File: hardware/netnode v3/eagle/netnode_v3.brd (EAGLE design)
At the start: 59.9 x 49.9 mm, 29 parts, among them IC1 TSR-1, IC2 PIC18F4K80, IC3 FOD060L, X1 DC10R, X2 XPORT

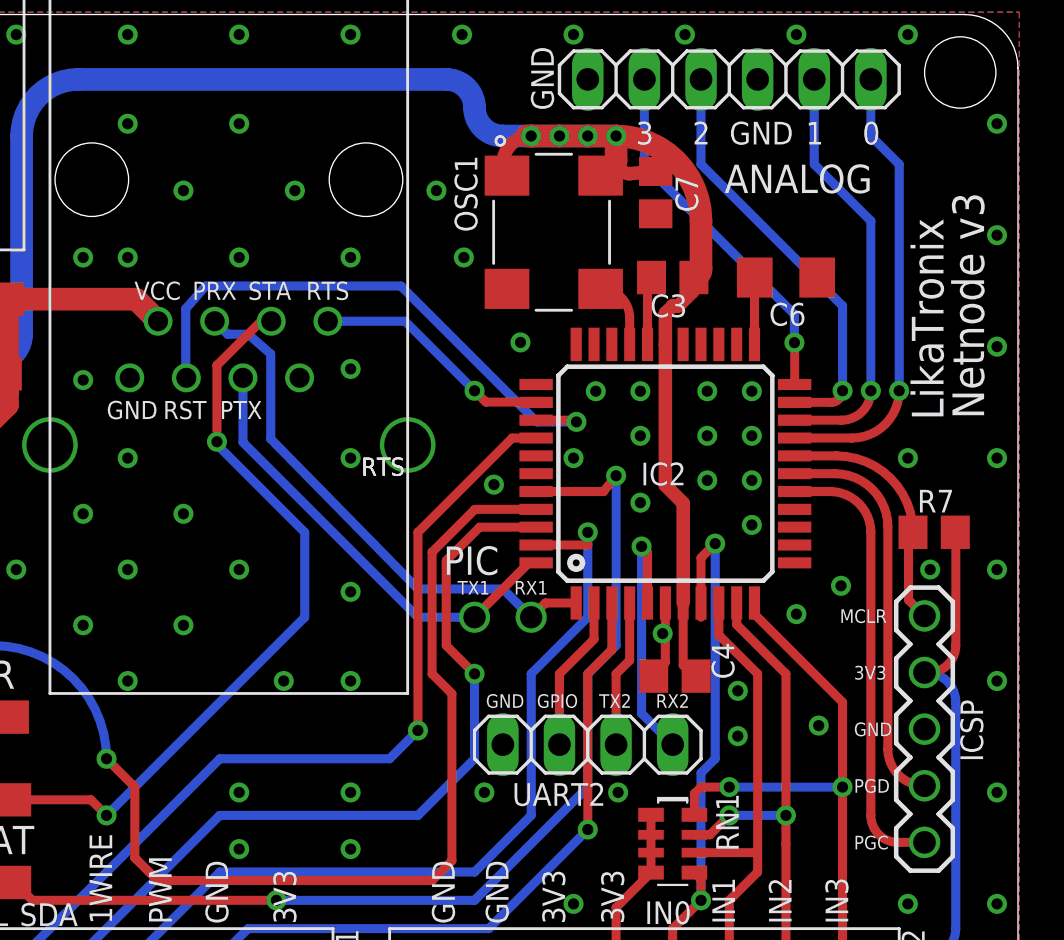
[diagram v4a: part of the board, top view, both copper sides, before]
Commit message: Added reset button.
The reset button from Wuerth is a handy addition when developing firmware.
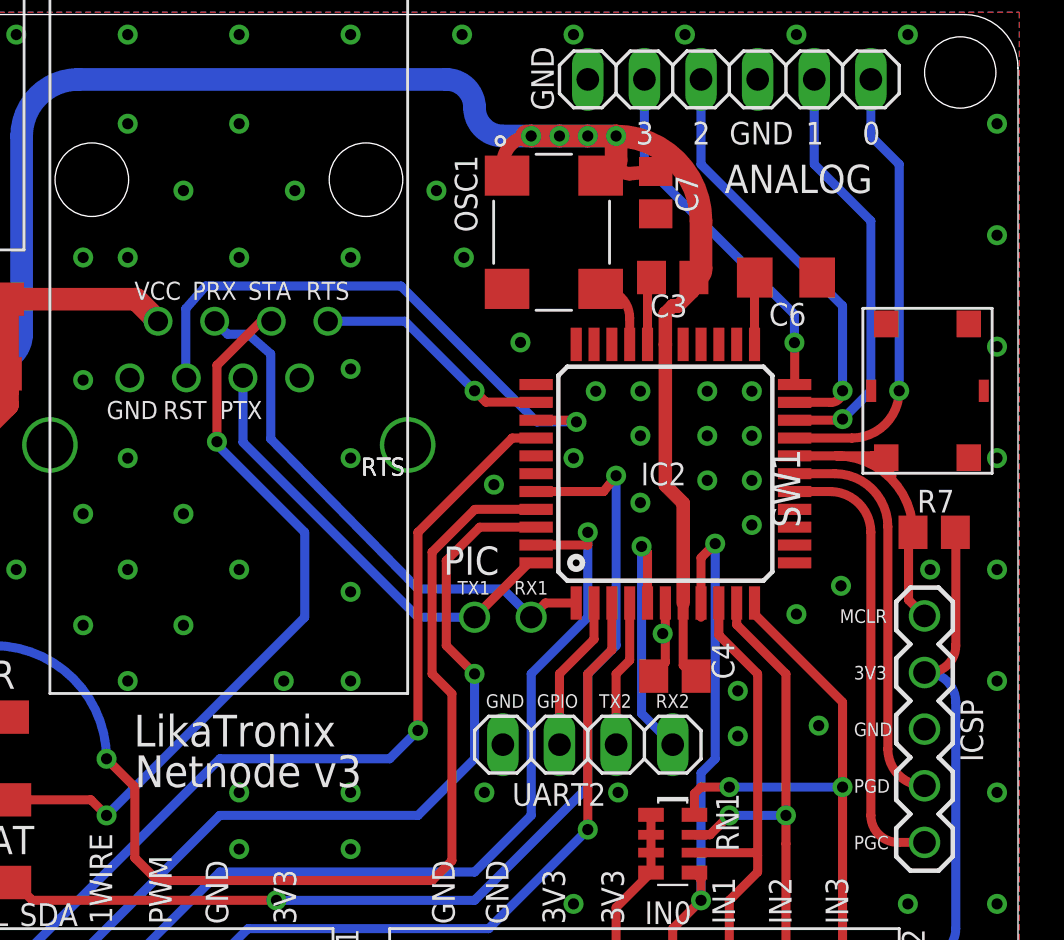
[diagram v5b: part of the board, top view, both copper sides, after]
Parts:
- added SW1: 431181015816, Eagle_Wuerth_Elektronik_Switch_Power_Elements:431181015816
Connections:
- net !MCLR: now also SW1.2
- net GND: now also SW1.1, SW1.GND@1, SW1.GND@2
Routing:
- net !MCLR: track 10.9 -> 14.6 mm
- net GND: vias 101 -> 100
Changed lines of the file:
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@@
 <?xml version="1.0" encoding="utf-8"?>
 <!DOCTYPE eagle SYSTEM "eagle.dtd">
-<eagle version="6.2">
+<eagle version="6.3">
 <drawing>
 <settings>
@@
 <text x="30.48" y="29.21" size="0.8128" layer="21" ratio="15">RTS</text>
 <text x="30.48" y="29.21" size="0.8128" layer="21" ratio="15">RTS</text>
-<text x="58.42" y="31.75" size="1.4224" layer="21" ratio="15" rot="R90">Netnode v3</text>
-<text x="56.6" y="31.7" size="1.4224" layer="21" ratio="15" rot="R90">LikaTronix</text>
+<text x="20.32" y="15.24" size="1.4224" layer="21" ratio="15">Netnode v3</text>
+<text x="20.27" y="17.06" size="1.4224" layer="21" ratio="15">LikaTronix</text>
 </plain>
 <attributes>
@@
 </class>
 </classes>
-<designrules>
+<designrules name="default">
 <description language="de">&lt;p&gt;
 &lt;b&gt;EAGLE design rules for the Eurocircuits STANDARD pool service 2-layer&lt;/b&gt;
@@
 <element name="R4" library="rcl" package="R0603" value="" x="17.78" y="2.921" rot="MR270"/>
 <element name="R5" library="rcl" package="R0603" value="" x="15.113" y="2.921" rot="MR270"/>
+<element name="SW1" library="Eagle_Wuerth_Elektronik_Switch_Power_Elements" package="431181015816" value="431181015816" x="55.88" y="33.02" rot="R90"/>
 </elements>
 <signals>
@@
 <via x="52" y="24.27" extent="1-16" drill="0.5"/>
 <via x="56" y="25" extent="1-16" drill="0.5"/>
-<via x="55" y="30" extent="1-16" drill="0.5"/>
 <via x="20" y="20" extent="1-16" drill="0.5"/>
 <via x="27" y="20" extent="1-16" drill="0.5"/>
@@
 <via x="36.43" y="28.81" extent="1-16" drill="0.5"/>
 <via x="21.87" y="7.36" extent="1-16" drill="0.5"/>
+<contactref element="SW1" pad="1"/>
+<contactref element="SW1" pad="GND@1"/>
+<contactref element="SW1" pad="GND@2"/>
 </signal>
 <signal name="VSUPPLY" class="1">
@@
 <wire x1="55.03" y1="23.636" x2="55.03" y2="26.47" width="0.4064" layer="1"/>
 <wire x1="55.03" y1="26.47" x2="55.23" y2="26.67" width="0.4064" layer="1" curve="-90"/>
+<contactref element="SW1" pad="2"/>
+<wire x1="54.03" y1="30.02" x2="54.03" y2="29.79" width="0.4064" layer="1"/>
+<wire x1="51.8" y1="30.1" x2="53.4" y2="30.1" width="0.4064" layer="1"/>
+<wire x1="53.4" y1="30.1" x2="54.29" y2="29.21" width="0.4064" layer="1"/>
+<wire x1="53.4" y1="30.1" x2="53.95" y2="30.1" width="0.4064" layer="1"/>
+<wire x1="53.95" y1="30.1" x2="54.03" y2="30.02" width="0.4064" layer="1"/>
 </signal>
 <signal name="PGD">
@@
 <contactref element="IC2" pad="20"/>
 <contactref element="ANALOG" pad="2"/>
-<via x="53.34" y="33.02" extent="1-16" drill="0.5"/>
-<wire x1="53.34" y1="33.02" x2="53.34" y2="40.64" width="0.4064" layer="16"/>
 <wire x1="53.34" y1="40.64" x2="50.8" y2="43.18" width="0.4064" layer="16"/>
 <wire x1="50.8" y1="43.18" x2="50.8" y2="46.99" width="0.4064" layer="16"/>
 <wire x1="49.92" y1="31.7" x2="52.02" y2="31.7" width="0.4064" layer="1"/>
-<wire x1="52.02" y1="31.7" x2="53.34" y2="33.02" width="0.4064" layer="1" curve="90"/>
+<wire x1="53.34" y1="40.64" x2="53.34" y2="33.02" width="0.4064" layer="16"/>
+<wire x1="53.34" y1="33.02" x2="52.07" y2="31.75" width="0.4064" layer="16"/>
+<wire x1="52.07" y1="31.75" x2="52.02" y2="31.7" width="0.4064" layer="16"/>
+<via x="52.07" y="31.75" extent="1-16" drill="0.5"/>
+<wire x1="52.02" y1="31.7" x2="52.02" y2="31.7" width="0" layer="19" extent="1-16"/>
 </signal>
 <signal name="AN2">

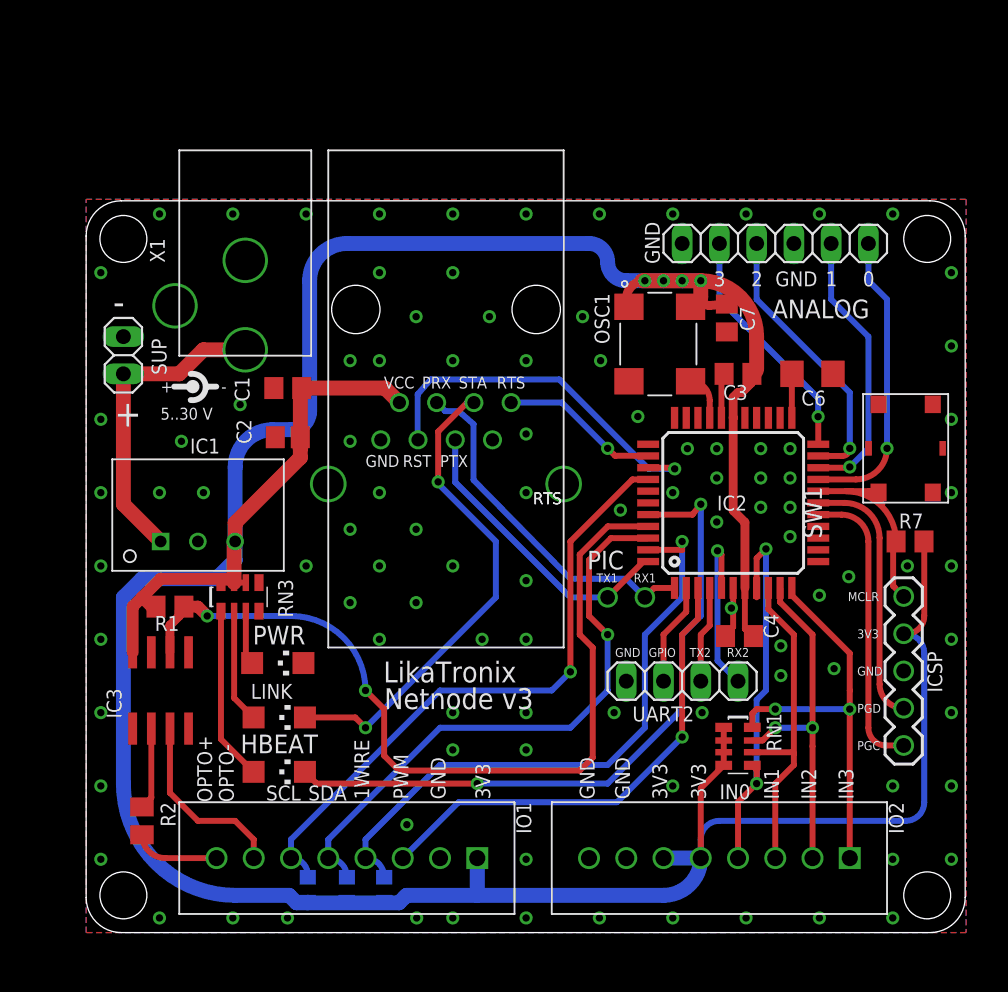
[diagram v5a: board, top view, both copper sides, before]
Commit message: Final fixes for boardout.
Added decoupling caps, fixed silkscreen, reviewed compontents
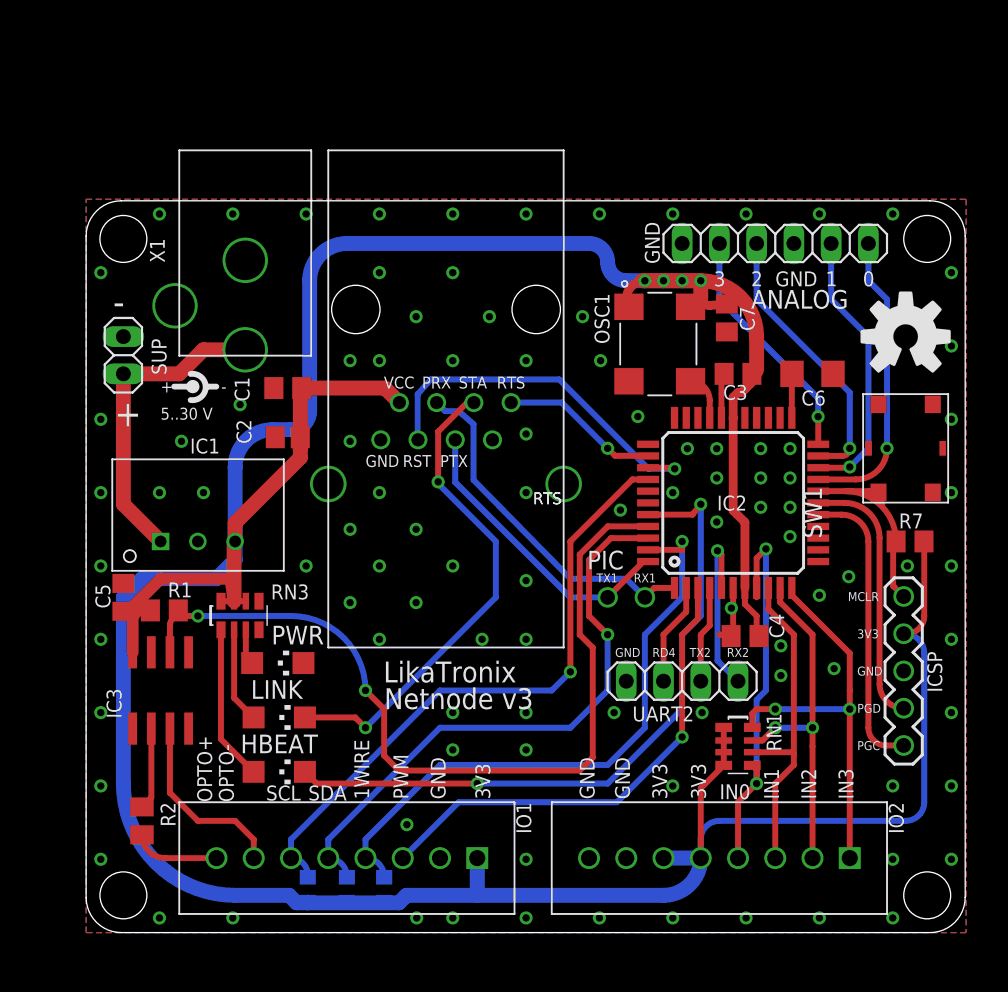
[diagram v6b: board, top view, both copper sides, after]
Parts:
- added C5: 100n, rcl:C0805
- moved RN3 1.27 mm to (10.5, 21.6)
- moved R1 0.46 mm to (5.33, 22.0)
- moved C4 0.38 mm to (44.9, 20.2)
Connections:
- net N$11 renamed VDDCAP
- net +3V3: now also C5.1
- net GND: now also C5.2
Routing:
- net +3V3: track 246.1 -> 249.9 mm
- net N$8: track 11.9 -> 10.6 mm
- net N$2: track 3.71 -> 2.44 mm
- net N$1: track 7.80 -> 6.53 mm
- net GND: track 6.95 -> 7.16 mm, vias 100 -> 99
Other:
- board text added: "ANALOG"
- board text added: "RD4"
- board text removed: "GPIO"

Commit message: Final gerber file commit of files sent to production. Fixed problems detected by PCB visualizer.
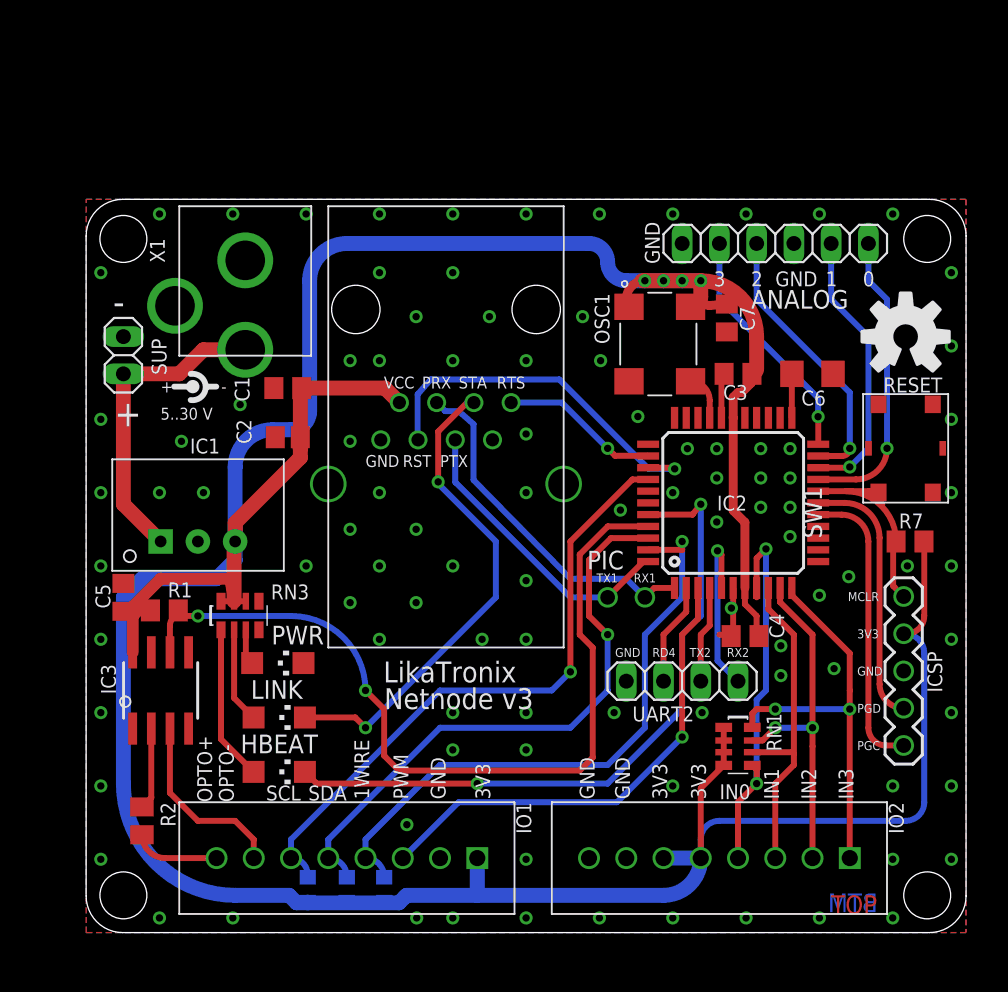
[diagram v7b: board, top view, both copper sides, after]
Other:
- board size 59.9 x 49.9 mm -> 60 x 50 mm
- board text added: "BTM"
- board text added: "RESET"
- board text added: "TOP"
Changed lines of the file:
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@@
 <?xml version="1.0" encoding="utf-8"?>
 <!DOCTYPE eagle SYSTEM "eagle.dtd">
-<eagle version="6.2">
+<eagle version="6.3">
 <drawing>
 <settings>
@@
 <setting verticaltext="up"/>
 </settings>
-<grid distance="1.27" unitdist="mm" unit="mm" style="lines" multiple="1" display="yes" altdistance="0.127" altunitdist="mm" altunit="mm"/>
+<grid distance="1" unitdist="mm" unit="mm" style="lines" multiple="1" display="yes" altdistance="0.5" altunitdist="mm" altunit="mm"/>
 <layers>
 <layer number="1" name="Top" color="4" fill="1" visible="yes" active="yes"/>
@@
 <layer number="20" name="Dimension" color="15" fill="1" visible="yes" active="yes"/>
 <layer number="21" name="tPlace" color="7" fill="1" visible="yes" active="yes"/>
-<layer number="22" name="bPlace" color="7" fill="1" visible="yes" active="yes"/>
+<layer number="22" name="bPlace" color="7" fill="1" visible="no" active="yes"/>
 <layer number="23" name="tOrigins" color="15" fill="1" visible="yes" active="yes"/>
 <layer number="24" name="bOrigins" color="15" fill="1" visible="no" active="yes"/>
@@
 <board>
 <plain>
-<wire x1="2.4" y1="0" x2="57.54" y2="0" width="0" layer="20"/>
 <hole x="2.54" y="2.54" drill="3.2"/>
 <text x="1.832" y="42.138" size="1.778" layer="21">-</text>
@@
 <text x="5.072" y="34.976" size="0.8128" layer="21">5..30 V</text>
 <text x="5.08" y="36.83" size="0.8128" layer="21">+</text>
-<wire x1="59.94" y1="2.4" x2="59.94" y2="47.5" width="0" layer="20"/>
-<wire x1="57.54" y1="49.9" x2="2.4" y2="49.9" width="0" layer="20"/>
-<wire x1="0" y1="47.5" x2="0" y2="2.4" width="0" layer="20"/>
 <wire x1="7.128" y1="38.092" x2="7.128" y2="36.314" width="0.4" layer="21" curve="-196.260205"/>
 <wire x1="6.004" y1="37.23" x2="7.274" y2="37.23" width="0.4" layer="21"/>
@@
 <hole x="57.35" y="47.3" drill="3.2"/>
 <hole x="57.35" y="2.54" drill="3.2"/>
-<wire x1="0" y1="47.5" x2="2.4" y2="49.9" width="0" layer="20" curve="-90"/>
-<wire x1="59.94" y1="2.4" x2="57.54" y2="0" width="0" layer="20" curve="-90"/>
-<wire x1="57.54" y1="49.9" x2="59.94" y2="47.5" width="0" layer="20" curve="-90"/>
-<wire x1="2.4" y1="0" x2="0" y2="2.4" width="0" layer="20" curve="-90"/>
 <text x="37.338" y="23.876" size="0.6096" layer="21" ratio="15">RX1</text>
 <text x="34.798" y="23.876" size="0.6096" layer="21" ratio="15">TX1</text>
@@
 <text x="25.4" y="37.1" size="0.8128" layer="21" ratio="15">STA</text>
 <text x="28" y="37.1" size="0.8128" layer="21" ratio="15">RTS</text>
-<text x="30.48" y="29.21" size="0.8128" layer="21" ratio="15">RTS</text>
-<text x="30.48" y="29.21" size="0.8128" layer="21" ratio="15">RTS</text>
 <text x="20.32" y="15.24" size="1.4224" layer="21" ratio="15">Netnode v3</text>
 <text x="20.27" y="17.06" size="1.4224" layer="21" ratio="15">LikaTronix</text>
@@
 <vertex x="56.238765625" y="39.7738625"/>
 </polygon>
+<text x="50.8" y="1.27" size="1.27" layer="1" ratio="15">TOP</text>
+<text x="53.975" y="1.397" size="1.27" layer="16" ratio="15" rot="MR0">BTM</text>
+<text x="54.356" y="36.83" size="1.016" layer="21" ratio="15">RESET</text>
+<wire x1="2.5" y1="0" x2="0" y2="2.5" width="0" layer="20" curve="-90"/>
+<wire x1="0" y1="2.5" x2="0" y2="47.5" width="0" layer="20"/>
+<wire x1="0" y1="47.5" x2="2.5" y2="50" width="0" layer="20" curve="-90"/>
+<wire x1="2.5" y1="50" x2="57.5" y2="50" width="0" layer="20"/>
+<wire x1="57.5" y1="50" x2="60" y2="47.5" width="0" layer="20" curve="-90"/>
+<wire x1="60" y1="47.5" x2="60" y2="2.5" width="0" layer="20"/>
+<wire x1="60" y1="2.5" x2="57.5" y2="0" width="0" layer="20" curve="-90"/>
+<wire x1="57.5" y1="0" x2="2.5" y2="0" width="0" layer="20"/>
 </plain>
 <attributes>
@@
 </class>
 </classes>
-<designrules>
+<designrules name="default">
 <description language="de">&lt;p&gt;
 &lt;b&gt;EAGLE design rules for the Eurocircuits STANDARD pool service 2-layer&lt;/b&gt;
@@
 </element>
 <element name="IC3" library="ic" package="SO-08" value="FOD060L" x="5.08" y="16.51" smashed="yes">
-<attribute name="NAME" x="2.413" y="14.605" size="1.016" layer="25" ratio="15" rot="R90"/>
+<attribute name="NAME" x="2.032" y="16.256" size="1.016" layer="25" ratio="15" rot="R90"/>
 <attribute name="VALUE" x="9.017" y="14.605" size="1.27" layer="27" rot="R90"/>
 </element>
